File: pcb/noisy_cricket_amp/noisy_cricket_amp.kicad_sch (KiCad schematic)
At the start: 16 parts

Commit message: Adding initial schematics
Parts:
- removed C?: C, symbol Device:C
- added C3: 100 nF, symbol Device:C
- added D1: LED, symbol Device:LED
- added J1: SJ1-3534, CUI_SJ1-3534, symbol SJ1-3534:SJ1-3534
- added J2: AudioJack2, symbol Connector:AudioJack2
- added Q1: MPF102, TO92F, symbol MPF102:MPF102
- added SW1, SW2: SW_SPST, symbol Switch:SW_SPST
- C1, C8: renamed from C?; value C_Polarized -> 220 uF
- C2, C7: renamed from C?; value C -> 47 nF
- C4, C5, C6: renamed from C?; value C -> 100 nF
- R1: renamed from R?; value R -> 1M
- R2: renamed from R?; value R -> 3k3
- R3: renamed from R?; value R -> 4k7
- R4: renamed from R?; value R -> 10
- RV1, RV2: renamed from RV?; value R_Potentiometer -> 1k
- RV3: renamed from RV?; value R_Potentiometer -> 100k
- gave numbers to parts that had none: 1
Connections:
- net at C7.1: now also R4.2
- net GND: now reaches C7.2
- net GND: now also C1.2, C5.2, R1.2, R2.2, RV1.1, U1.3 (+), U1.4 (GND), C3.2, D1.1 (K), J1.1, J2.S
- net at C8.1: now also C4.2, R4.1, U1.5
- net at C8.2: now also J2.T
- net at C6.1: now also U1.2 (-)
- net at C6.2: now also RV1.2, RV3.1
- net at R3.1: now also C1.1, U1.6 (V+), Q1.1, SW1.2 (B)
- net at R3.2: now also D1.2 (A)
- net at RV2.1: now also RV2.2, U1.1 (GAIN)
- net at RV2.3: now also U1.8 (GAIN)
- net at C2.1: now also RV1.3
- net at C2.2: now also R2.1, Q1.2
- net at C4.1: now also SW2.2 (B)
- net at RV3.2: now also C5.1, RV3.3
- net at R1.1: now also J1.2, J1.3, Q1.3
- net at U1.7 (BYPASS): now also C3.1, SW2.1 (A)
- new net +9V: SW1.1 (A)
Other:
- moved on the sheet: C1, C2, C4, C5, C6, C7, C8, R1, R2, R3, R4, RV1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

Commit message: Adding component footprints
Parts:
- added J3: Jack-DC, Connector_Wire:SolderWire-0.5sqmm_1x02_P4.8mm_D0.9mm_OD2.3mm, symbol Connector:Jack-DC
- C1, C8: footprint (none) -> Capacitor_THT:CP_Radial_Tantal_D8.0mm_P5.00mm
- C2, C3, C4, C5, C6, C7: footprint (none) -> Capacitor_THT:C_Rect_L7.0mm_W2.0mm_P5.00mm
- J2, SW1, SW2: footprint (none) -> Connector_Wire:SolderWire-0.5sqmm_1x02_P4.8mm_D0.9mm_OD2.3mm
- R1, R2: footprint (none) -> Resistor_THT:R_Box_L8.4mm_W2.5mm_P5.08mm
- RV1, RV2, RV3: footprint (none) -> Potentiometer_THT:Potentiometer_Vishay_T73XW_Horizontal
- U1: footprint (none) -> LM386:DIL08
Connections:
- net GND: now also J3.2
- net +9V: no longer names the net of SW1.1 (A)
- net +9V: now also J3.1

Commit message: Initial pcb placement
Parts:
- removed J1: SJ1-3534, CUI_SJ1-3534, symbol SJ1-3534:SJ1-3534
- added J1: AudioJack2, Connector_Wire:SolderWire-0.5sqmm_1x02_P4.8mm_D0.9mm_OD2.3mm, symbol Connector:AudioJack2
- D1: footprint (none) -> LED_THT:LED_D3.0mm
- R3, R4: footprint (none) -> Resistor_THT:R_Box_L8.4mm_W2.5mm_P5.08mm
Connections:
- net GND: now also J1.S
- net at Q1.3, R1.1: now also J1.T

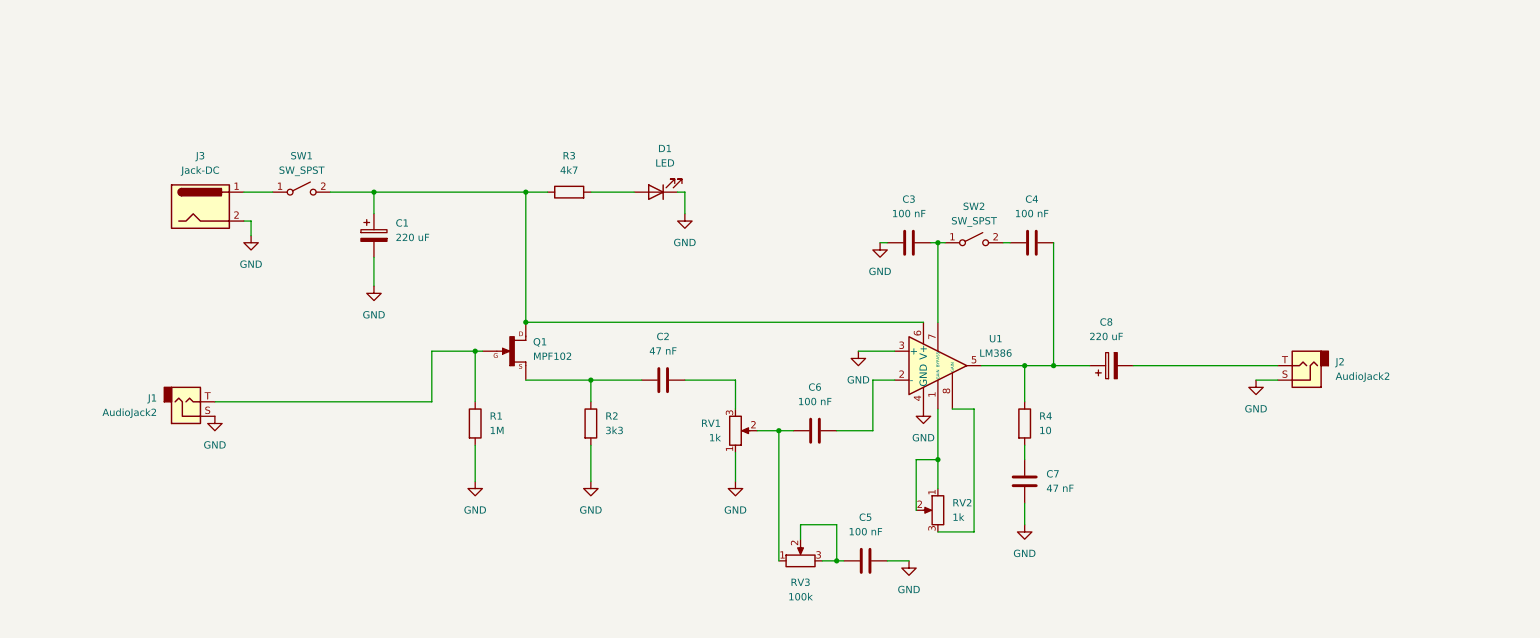
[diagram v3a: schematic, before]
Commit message: Adding p10 output connector and initial pcb placement
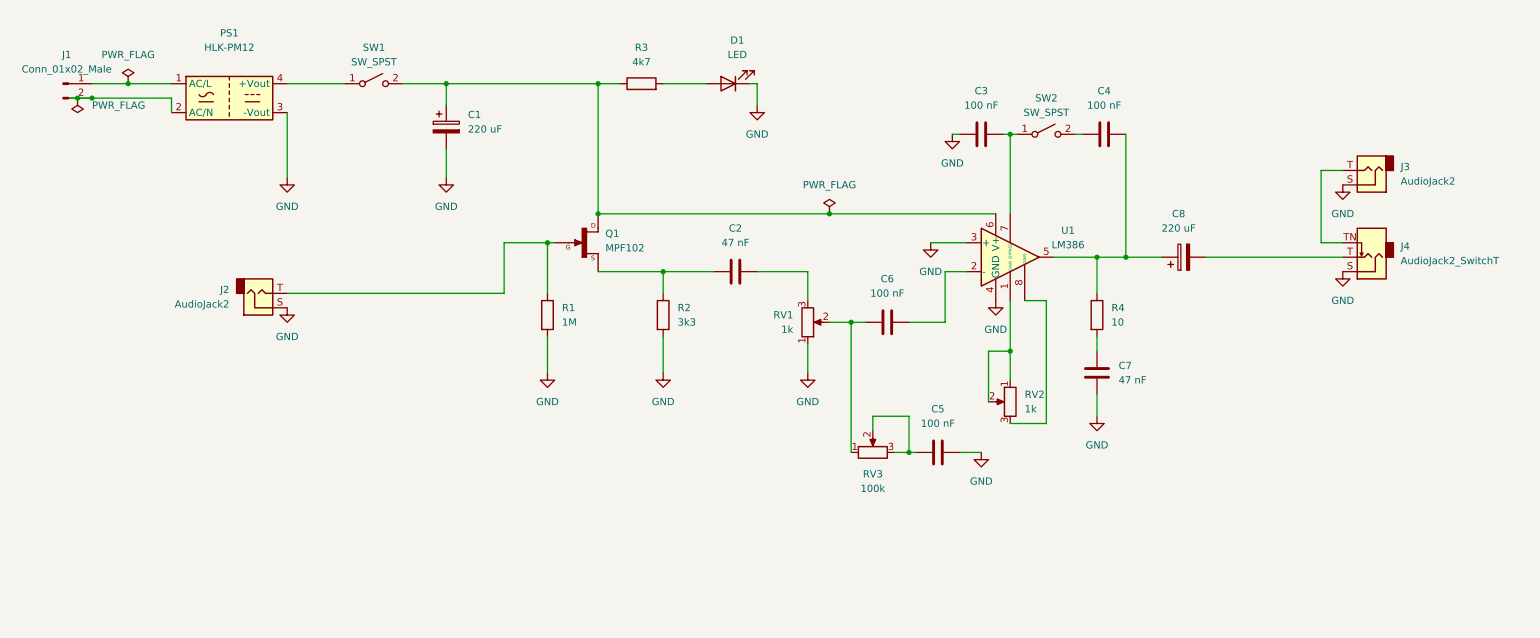
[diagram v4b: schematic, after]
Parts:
- removed J2: AudioJack2, Connector_Wire:SolderWire-0.5sqmm_1x02_P4.8mm_D0.9mm_OD2.3mm, symbol Connector:AudioJack2
- removed J3: Jack-DC, Connector_Wire:SolderWire-0.5sqmm_1x02_P4.8mm_D0.9mm_OD2.3mm, symbol Connector:Jack-DC
- added J1: Conn_01x02_Male, Connector_Wire:SolderWire-0.1sqmm_1x02_P3.6mm_D0.4mm_OD1mm, symbol Connector:Conn_01x02_Male
- added J3: AudioJack2, Connector_Wire:SolderWire-0.5sqmm_1x02_P4.8mm_D0.9mm_OD2.3mm, symbol Connector:AudioJack2
- added J4: AudioJack2_SwitchT, Connector_Wire:SolderWire-0.5sqmm_1x03_P4.8mm_D0.9mm_OD2.3mm, symbol Connector:AudioJack2_SwitchT
- added PS1: HLK-PM12, Converter_ACDC:Converter_ACDC_HiLink_HLK-PMxx, symbol Converter_ACDC:HLK-PM12
- renumbered J1 to J2
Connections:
- net GND: now also J3.S, J4.S, PS1.3 (-Vout)
- net at C8.2: now also J4.T
- net at SW1.1 (A): now also PS1.4 (+Vout)
- new net: J1.1 (Pin_1), PS1.1 (AC/L)
- new net: J1.2 (Pin_2), PS1.2 (AC/N)
- new net: J3.T, J4.TN
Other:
- moved on the sheet: C1, C2, C3, C4, C5, C6, C7, C8, D1, J2, Q1, R1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

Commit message: Routing component trails
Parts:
- added H1, H2, H3, H4: MountingHole, MountingHole:MountingHole_2.2mm_M2, symbol Mechanical:MountingHole
- J1: footprint Connector_Wire:SolderWire-0.1sqmm_1x02_P3.6mm_D0.4mm_OD1mm -> Connector_Wire:SolderWire-0.5sqmm_1x02_P4.8mm_D0.9mm_OD2.3mm
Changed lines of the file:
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@@
   (symbol (lib_id "power:GND") (at 255.27 57.15 0) (unit 1)
     (in_bom yes) (on_board yes) (fields_autoplaced)
-    (property "Reference" "#PWR?" (id 0) (at 255.27 63.5 0)
+    (property "Reference" "#PWR0113" (id 0) (at 255.27 63.5 0)
       (effects (font (size 1.27 1.27)) hide)
     )
@@
     (pin "2")
   )
+  (symbol (lib_id "Mechanical:MountingHole") (at 41.91 116.84 0) (unit 1)
+    (in_bom yes) (on_board yes) (fields_autoplaced)
+    (property "Reference" "H2" (id 0) (at 44.45 115.5699 0)
+      (effects (font (size 1.27 1.27)) (justify left))
+    )
+    (property "Value" "MountingHole" (id 1) (at 44.45 118.1099 0)
+      (effects (font (size 1.27 1.27)) (justify left))
+    )
+    (property "Footprint" "MountingHole:MountingHole_2.2mm_M2" (id 2) (at 41.91 116.84 0)
+      (effects (font (size 1.27 1.27)) hide)
+    )
+    (property "Datasheet" "~" (id 3) (at 41.91 116.84 0)
+      (effects (font (size 1.27 1.27)) hide)
+    )
+  )
   (symbol (lib_id "power:GND") (at 186.69 48.26 0) (unit 1)
     (in_bom yes) (on_board yes) (fields_autoplaced)
@@
     (pin "1")
   )
+  (symbol (lib_id "Mechanical:MountingHole") (at 41.91 124.46 0) (unit 1)
+    (in_bom yes) (on_board yes) (fields_autoplaced)
+    (property "Reference" "H3" (id 0) (at 44.45 123.1899 0)
+      (effects (font (size 1.27 1.27)) (justify left))
+    )
+    (property "Value" "MountingHole" (id 1) (at 44.45 125.7299 0)
+      (effects (font (size 1.27 1.27)) (justify left))
+    )
+    (property "Footprint" "MountingHole:MountingHole_2.2mm_M2" (id 2) (at 41.91 124.46 0)
+      (effects (font (size 1.27 1.27)) hide)
+    )
+    (property "Datasheet" "~" (id 3) (at 41.91 124.46 0)
+      (effects (font (size 1.27 1.27)) hide)
+    )
+  )
   (symbol (lib_id "power:GND") (at 97.79 55.88 0) (unit 1)
     (in_bom yes) (on_board yes) (fields_autoplaced)
@@
   (symbol (lib_id "power:GND") (at 255.27 72.39 0) (unit 1)
     (in_bom yes) (on_board yes) (fields_autoplaced)
-    (property "Reference" "#PWR?" (id 0) (at 255.27 78.74 0)
+    (property "Reference" "#PWR0114" (id 0) (at 255.27 78.74 0)
       (effects (font (size 1.27 1.27)) hide)
     )
@@
     (property "Reference" "J1" (id 0) (at 31.115 34.29 0))
     (property "Value" "Conn_01x02_Male" (id 1) (at 31.115 36.83 0))
-    (property "Footprint" "Connector_Wire:SolderWire-0.1sqmm_1x02_P3.6mm_D0.4mm_OD1mm" (id 2) (at 30.48 39.37 0)
+    (property "Footprint" "Connector_Wire:SolderWire-0.5sqmm_1x02_P4.8mm_D0.9mm_OD2.3mm" (id 2) (at 30.48 39.37 0)
       (effects (font (size 1.27 1.27)) hide)
     )
@@
     (pin "3")
   )
+  (symbol (lib_id "Mechanical:MountingHole") (at 41.91 132.08 0) (unit 1)
+    (in_bom yes) (on_board yes) (fields_autoplaced)
+    (property "Reference" "H4" (id 0) (at 44.45 130.8099 0)
+      (effects (font (size 1.27 1.27)) (justify left))
+    )
+    (property "Value" "MountingHole" (id 1) (at 44.45 133.3499 0)
+      (effects (font (size 1.27 1.27)) (justify left))
+    )
+    (property "Footprint" "MountingHole:MountingHole_2.2mm_M2" (id 2) (at 41.91 132.08 0)
+      (effects (font (size 1.27 1.27)) hide)
+    )
+    (property "Datasheet" "~" (id 3) (at 41.91 132.08 0)
+      (effects (font (size 1.27 1.27)) hide)
+    )
+  )
   (symbol (lib_id "Device:C") (at 191.77 48.26 270) (unit 1)
     (in_bom yes) (on_board yes) (fields_autoplaced)
@@
     )
     (pin "1")
+  )
+  (symbol (lib_id "Mechanical:MountingHole") (at 41.91 109.22 0) (unit 1)
+    (in_bom yes) (on_board yes) (fields_autoplaced)
+    (property "Reference" "H1" (id 0) (at 44.45 107.9499 0)
+      (effects (font (size 1.27 1.27)) (justify left))
+    )
+    (property "Value" "MountingHole" (id 1) (at 44.45 110.4899 0)
+      (effects (font (size 1.27 1.27)) (justify left))
+    )
+    (property "Footprint" "MountingHole:MountingHole_2.2mm_M2" (id 2) (at 41.91 109.22 0)
+      (effects (font (size 1.27 1.27)) hide)
+    )
+    (property "Datasheet" "~" (id 3) (at 41.91 109.22 0)
+      (effects (font (size 1.27 1.27)) hide)
+    )
   )
   (symbol (lib_id "power:GND") (at 212.09 97.79 0) (unit 1)
@@
     )
     (path "/0dc004c8-74d0-4773-baa6-931817f663f0"
-      (reference "#PWR?") (unit 1) (value "GND") (footprint "")
+      (reference "#PWR0113") (unit 1) (value "GND") (footprint "")
     )
     (path "/5a7aa792-163a-45b9-978b-d55e6d8c509a"
-      (reference "#PWR?") (unit 1) (value "GND") (footprint "")
+      (reference "#PWR0114") (unit 1) (value "GND") (footprint "")
     )
     (path "/d58c0414-b9c5-4a7d-aaee-9e8ef4ac3010"
@@
       (reference "D1") (unit 1) (value "LED") (footprint "LED_THT:LED_D3.0mm")
     )
+    (path "/bd695a2a-202a-4332-9c71-e8ce90870bd2"
+      (reference "H1") (unit 1) (value "MountingHole") (footprint "MountingHole:MountingHole_2.2mm_M2")
+    )
+    (path "/2e77b784-f421-4476-9a99-77878d24a4ea"
+      (reference "H2") (unit 1) (value "MountingHole") (footprint "MountingHole:MountingHole_2.2mm_M2")
+    )
+    (path "/546801e4-4648-48e5-819a-6e0f15ba37d1"
+      (reference "H3") (unit 1) (value "MountingHole") (footprint "MountingHole:MountingHole_2.2mm_M2")
+    )
+    (path "/6d28f7a9-e3c4-4cc6-a9e1-a8d22f58579e"
+      (reference "H4") (unit 1) (value "MountingHole") (footprint "MountingHole:MountingHole_2.2mm_M2")
+    )
     (path "/5c0a3b05-f809-4d2b-80d6-832289163970"
-      (reference "J1") (unit 1) (value "Conn_01x02_Male") (footprint "Connector_Wire:SolderWire-0.1sqmm_1x02_P3.6mm_D0.4mm_OD1mm")
+      (reference "J1") (unit 1) (value "Conn_01x02_Male") (footprint "Connector_Wire:SolderWire-0.5sqmm_1x02_P4.8mm_D0.9mm_OD2.3mm")
     )
     (path "/7b301ee2-e729-452f-9845-d269f4d28af0"

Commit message: Holes for battery and layout improvements
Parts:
- added H5, H6: MountingHole_Pad, MountingHole:MountingHole_2.1mm, symbol Mechanical:MountingHole_Pad
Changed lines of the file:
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@@
+    (pin "1")
+  )
+  (symbol (lib_id "Mechanical:MountingHole_Pad") (at 69.85 127 0) (unit 1)
+    (in_bom yes) (on_board yes) (fields_autoplaced)
+    (property "Reference" "H6" (id 0) (at 72.39 124.4599 0)
+      (effects (font (size 1.27 1.27)) (justify left))
+    )
+    (property "Value" "MountingHole_Pad" (id 1) (at 72.39 126.9999 0)
+      (effects (font (size 1.27 1.27)) (justify left))
+    )
+    (property "Footprint" "MountingHole:MountingHole_2.1mm" (id 2) (at 69.85 127 0)
+      (effects (font (size 1.27 1.27)) hide)
+    )
+    (property "Datasheet" "~" (id 3) (at 69.85 127 0)
+      (effects (font (size 1.27 1.27)) hide)
+    )
     (pin "1")
   )
@@
     (pin "8")
   )
+  (symbol (lib_id "Mechanical:MountingHole_Pad") (at 69.85 113.03 0) (unit 1)
+    (in_bom yes) (on_board yes) (fields_autoplaced)
+    (property "Reference" "H5" (id 0) (at 72.39 110.4899 0)
+      (effects (font (size 1.27 1.27)) (justify left))
+    )
+    (property "Value" "MountingHole_Pad" (id 1) (at 72.39 113.0299 0)
+      (effects (font (size 1.27 1.27)) (justify left))
+    )
+    (property "Footprint" "MountingHole:MountingHole_2.1mm" (id 2) (at 69.85 113.03 0)
+      (effects (font (size 1.27 1.27)) hide)
+    )
+    (property "Datasheet" "~" (id 3) (at 69.85 113.03 0)
+      (effects (font (size 1.27 1.27)) hide)
+    )
+    (pin "1")
+  )
   (symbol (lib_id "Device:C_Polarized") (at 97.79 46.99 0) (unit 1)
     (in_bom yes) (on_board yes) (fields_autoplaced)
@@
       (reference "H4") (unit 1) (value "MountingHole") (footprint "MountingHole:MountingHole_2.2mm_M2")
     )
+    (path "/d25f8ef4-1d94-4d66-aea1-369c25550fd4"
+      (reference "H5") (unit 1) (value "MountingHole_Pad") (footprint "MountingHole:MountingHole_2.1mm")
+    )
+    (path "/54439a6c-ea9c-434f-b3bb-57c6d95db7ad"
+      (reference "H6") (unit 1) (value "MountingHole_Pad") (footprint "MountingHole:MountingHole_2.1mm")
+    )
     (path "/5c0a3b05-f809-4d2b-80d6-832289163970"
